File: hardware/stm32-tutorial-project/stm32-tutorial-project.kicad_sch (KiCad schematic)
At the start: 25 parts, among them J2 10pin IDC SWD, SW1 SW_Push, SW2 SW_Push_SPDT, U1 STM32G431CBTx

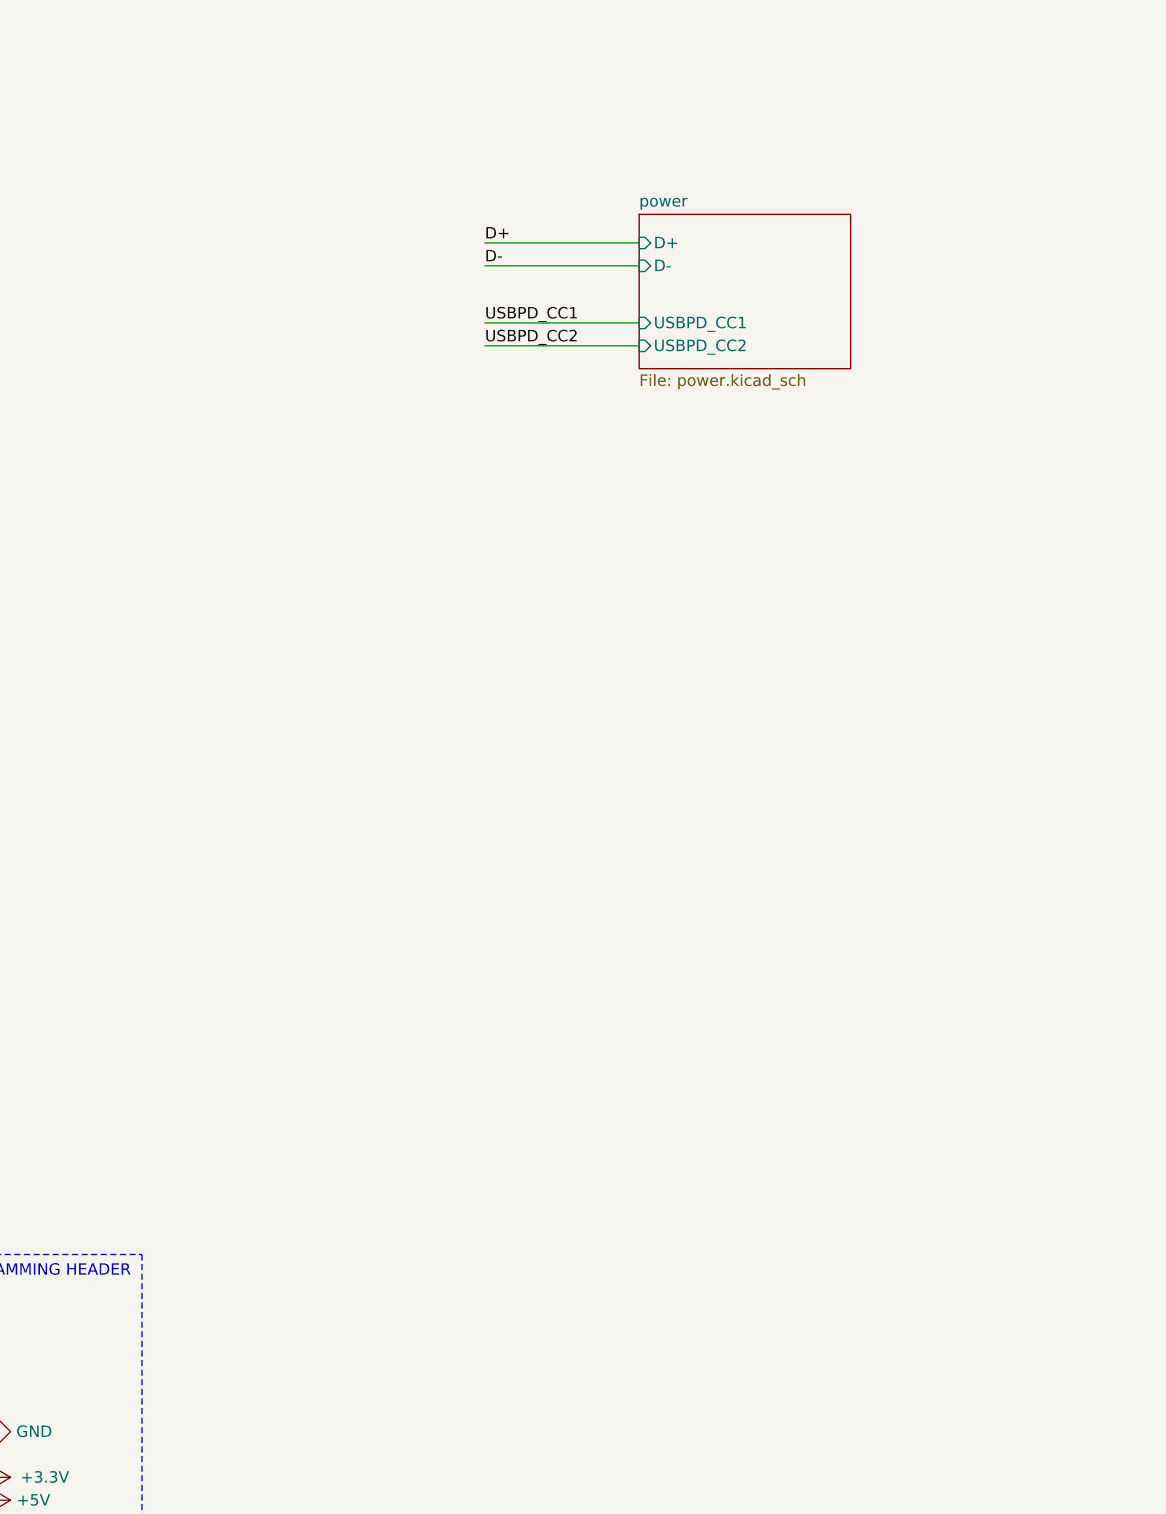
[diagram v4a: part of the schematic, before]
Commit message: added debug leds
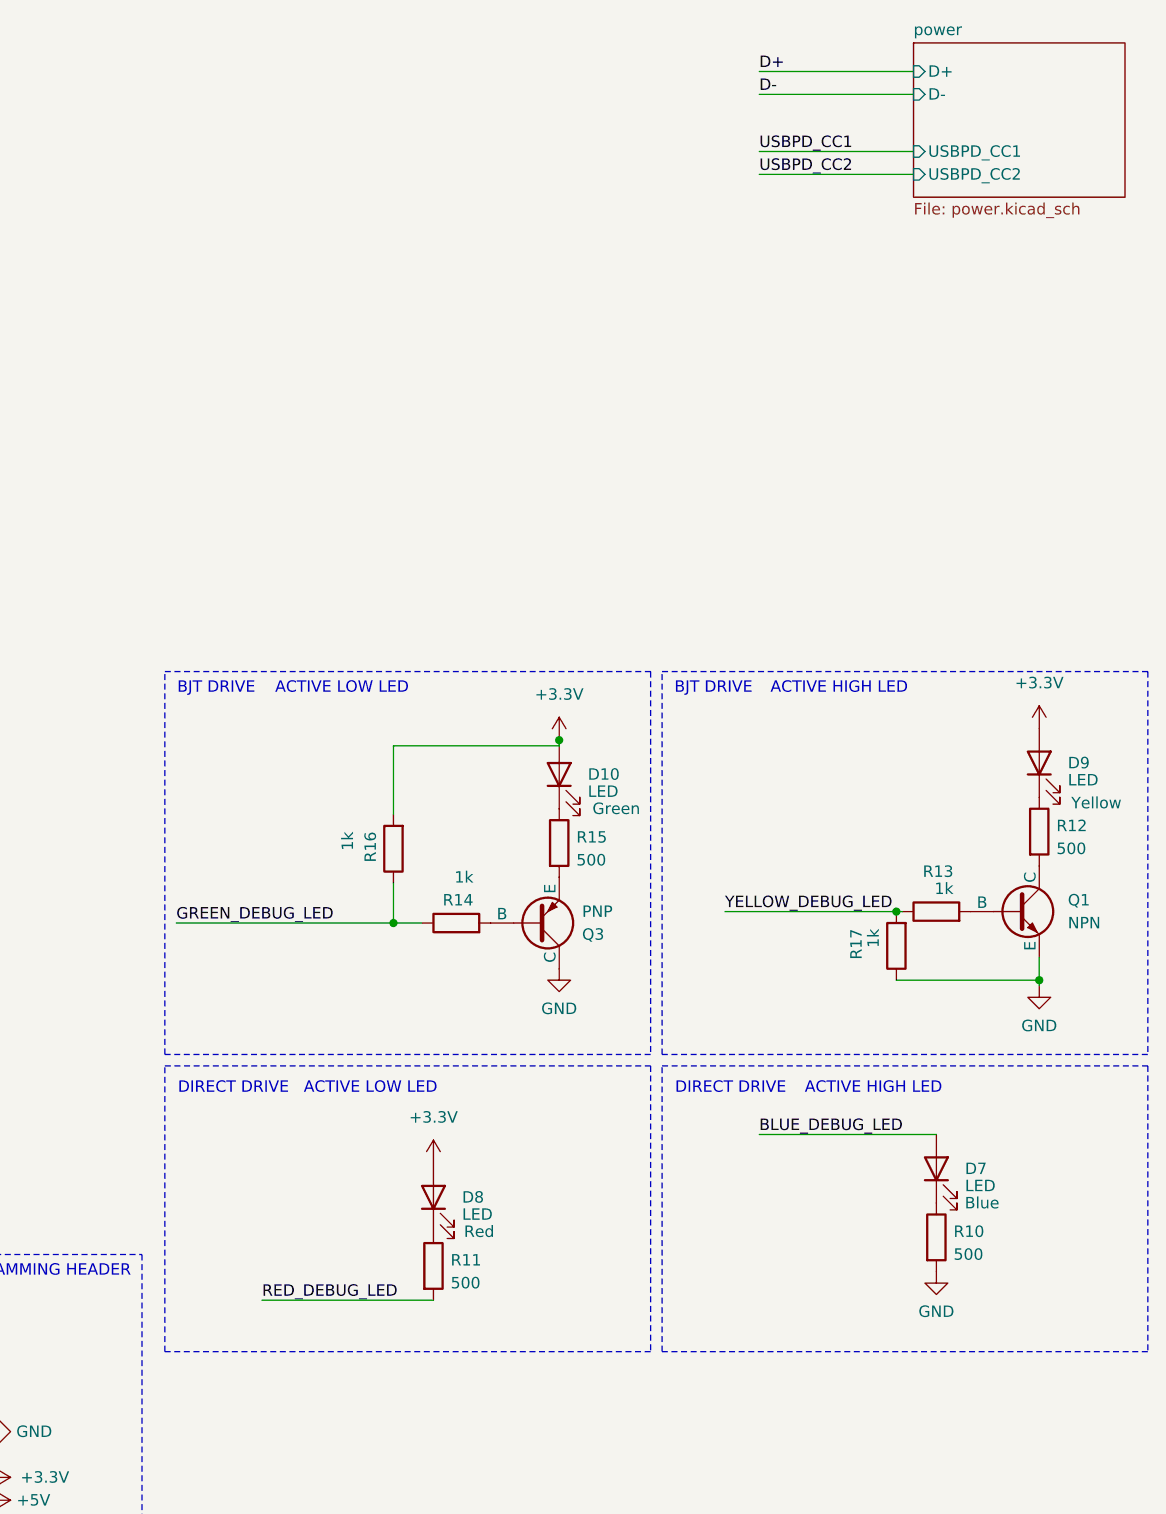
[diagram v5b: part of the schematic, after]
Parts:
- added D10, D7, D8, D9: LED, symbol Device:LED
- added Q1: NPN, symbol Simulation_SPICE:NPN
- added Q3: PNP, symbol Simulation_SPICE:PNP
- added R10, R11, R12, R15: 500, symbol Device:R
- added R13, R14, R16, R17: 1k, symbol Device:R
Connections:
- net +3.3V: now also D10.2 (A), D8.2 (A), D9.2 (A), R16.2
- net GND: now also Q1.3 (E), Q3.1 (C), R10.2, R17.1
- new net: D7.1 (K), R10.1
- new net: Q1.2 (B), R13.2
- new net: D8.1 (K), R11.1
- new net: D9.1 (K), R12.1
- new net: Q1.1 (C), R12.2
- new net: D10.1 (K), R15.1
- new net: Q3.3 (E), R15.2
- new net: Q3.2 (B), R14.2
- new net BLUE_DEBUG_LED: D7.2 (A)
- new net GREEN_DEBUG_LED: R14.1, R16.1
- new net RED_DEBUG_LED: R11.2
- new net YELLOW_DEBUG_LED: R13.1, R17.2
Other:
- note added: "ACTIVE HIGH LED"
- note added: "ACTIVE LOW LED"
- note added: "BJT DRIVE"
- note added: "DIRECT DRIVE"

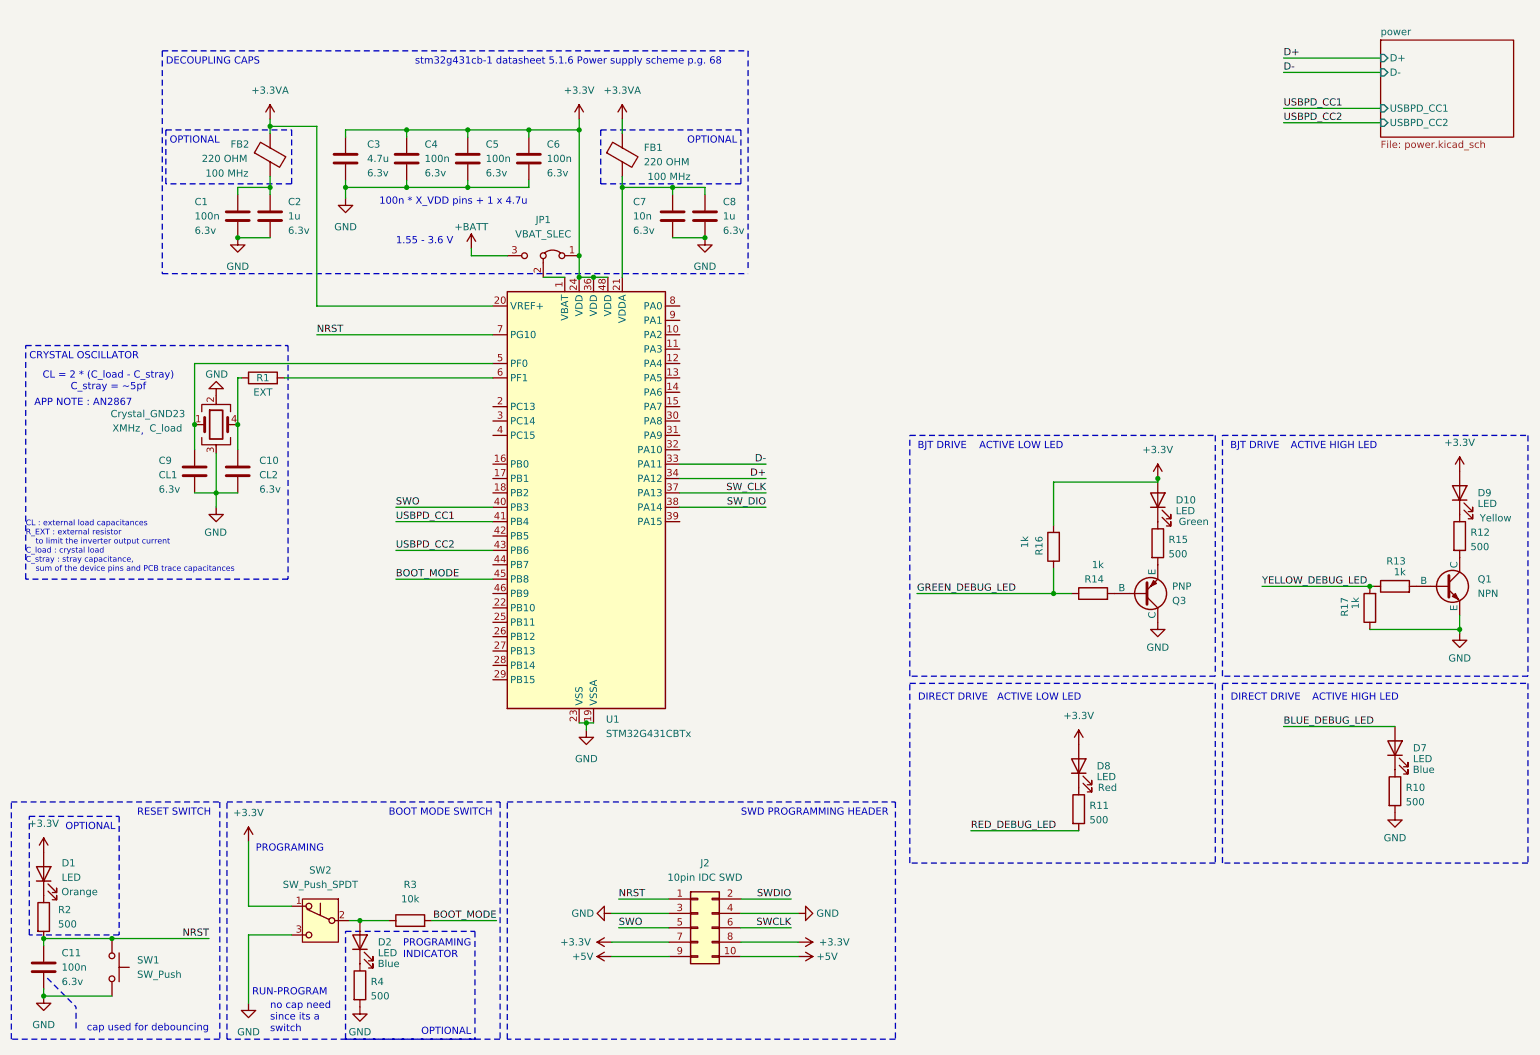
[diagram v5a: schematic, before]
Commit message: added connectors for distance sensors
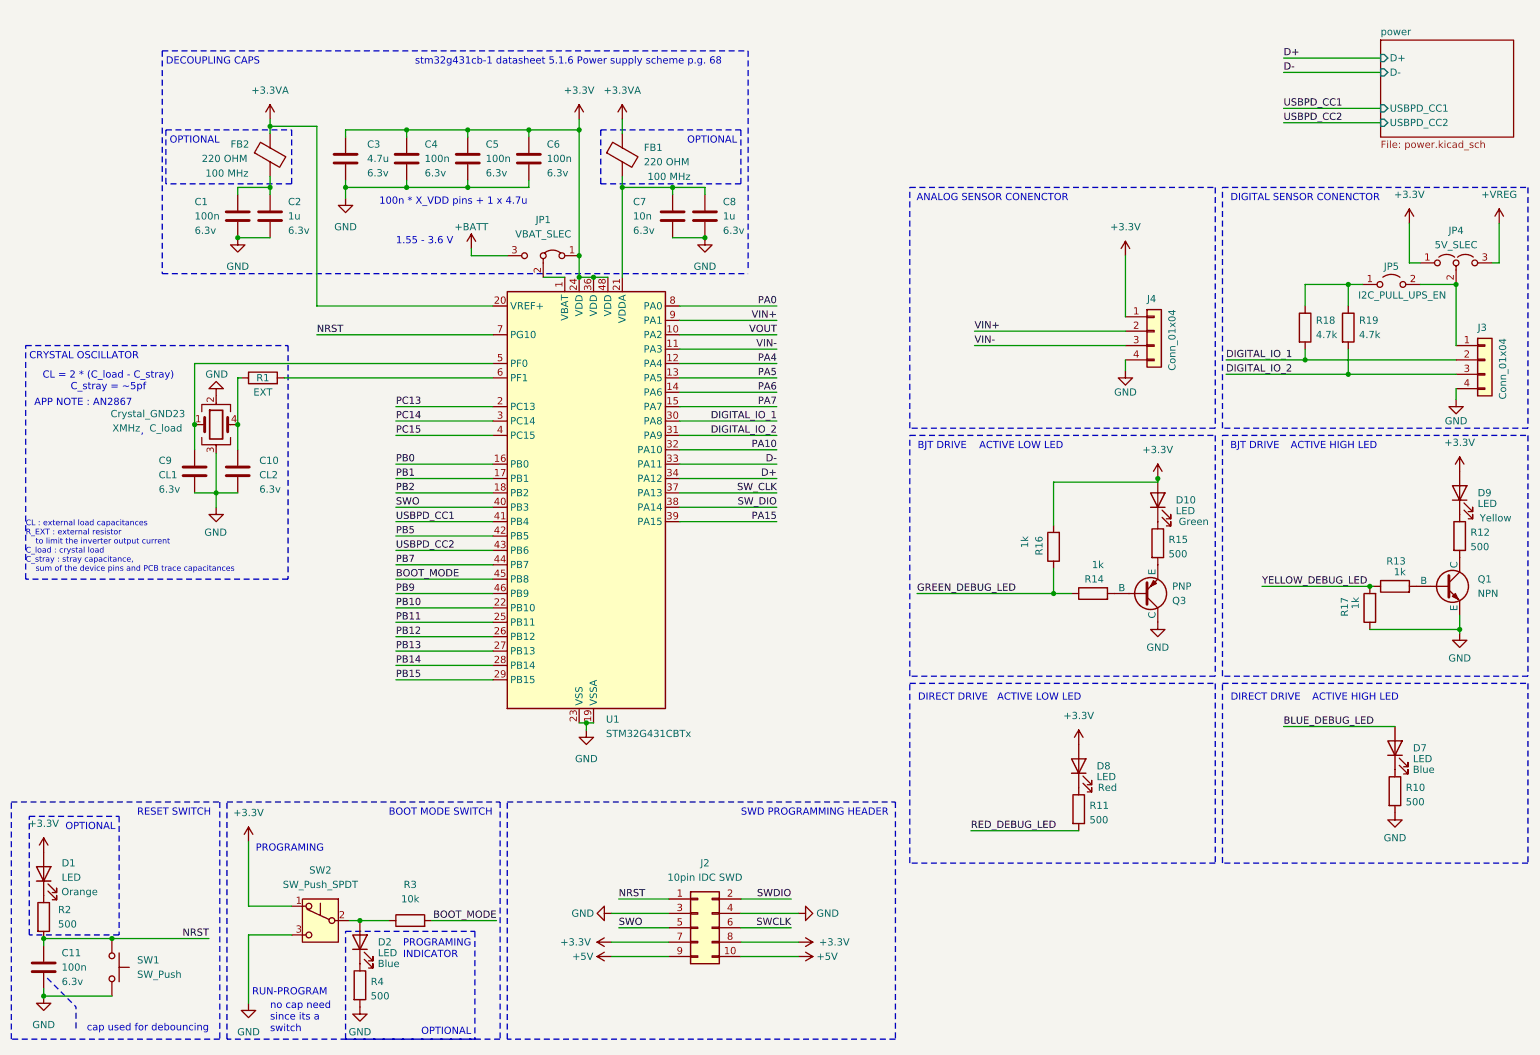
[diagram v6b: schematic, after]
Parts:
- added J3, J4: Conn_01x04, 4ms_Connector:Pins_1x04_2.54mm_TH_SWD, symbol PCM_4ms_Connector:Conn_01x04
- added JP4: 5V_SLEC, symbol Jumper:Jumper_3_Open
- added JP5: I2C_PULL_UPS_EN, symbol Jumper:Jumper_2_Open
- added R18, R19: 4.7k, symbol Device:R
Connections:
- net +3.3V: now also J4.1 (Pin_1), JP4.1 (A)
- net GND: now also J3.4 (Pin_4), J4.4 (Pin_4)
- net VOUT: now reaches U1.10 (PA2)
- net VIN-: now reaches U1.11 (PA3)
- net VIN-: now also J4.3 (Pin_3)
- net PA4: now reaches U1.12 (PA4)
- net PA5: now reaches U1.13 (PA5)
- net PA6: now reaches U1.14 (PA6)
- net PA7: now reaches U1.15 (PA7)
- net PB0: now reaches U1.16 (PB0)
- net PB1: now reaches U1.17 (PB1)
- net PB2: now reaches U1.18 (PB2)
- net PC13: now reaches U1.2 (PC13)
- net PB10: now reaches U1.22 (PB10)
- net PB11: now reaches U1.25 (PB11)
- net PB12: now reaches U1.26 (PB12)
- net PB13: now reaches U1.27 (PB13)
- net PB14: now reaches U1.28 (PB14)
- net PB15: now reaches U1.29 (PB15)
- net PC14: now reaches U1.3 (PC14)
- net DIGITAL_IO_1: now reaches U1.30 (PA8)
- net DIGITAL_IO_1: now also J3.2 (Pin_2), R18.2
- net DIGITAL_IO_2: now reaches U1.31 (PA9)
- net DIGITAL_IO_2: now also J3.3 (Pin_3), R19.2
- net PA10: now reaches U1.32 (PA10)
- net PA15: now reaches U1.39 (PA15)
- net PC15: now reaches U1.4 (PC15)
- net PB5: now reaches U1.42 (PB5)
- net PB7: now reaches U1.44 (PB7)
- net PB9: now reaches U1.46 (PB9)
- net PA0: now reaches U1.8 (PA0)
- net VIN+: now reaches U1.9 (PA1)
- net VIN+: now also J4.2 (Pin_2)
- new net: J3.1 (Pin_1), JP4.2 (C), JP5.2 (B)
- new net: JP5.1 (A), R18.1, R19.1
- new net +VREG: JP4.3 (B)
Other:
- note added: "ANALOG SENSOR CONENCTOR"
- note added: "DIGITAL SENSOR CONENCTOR"

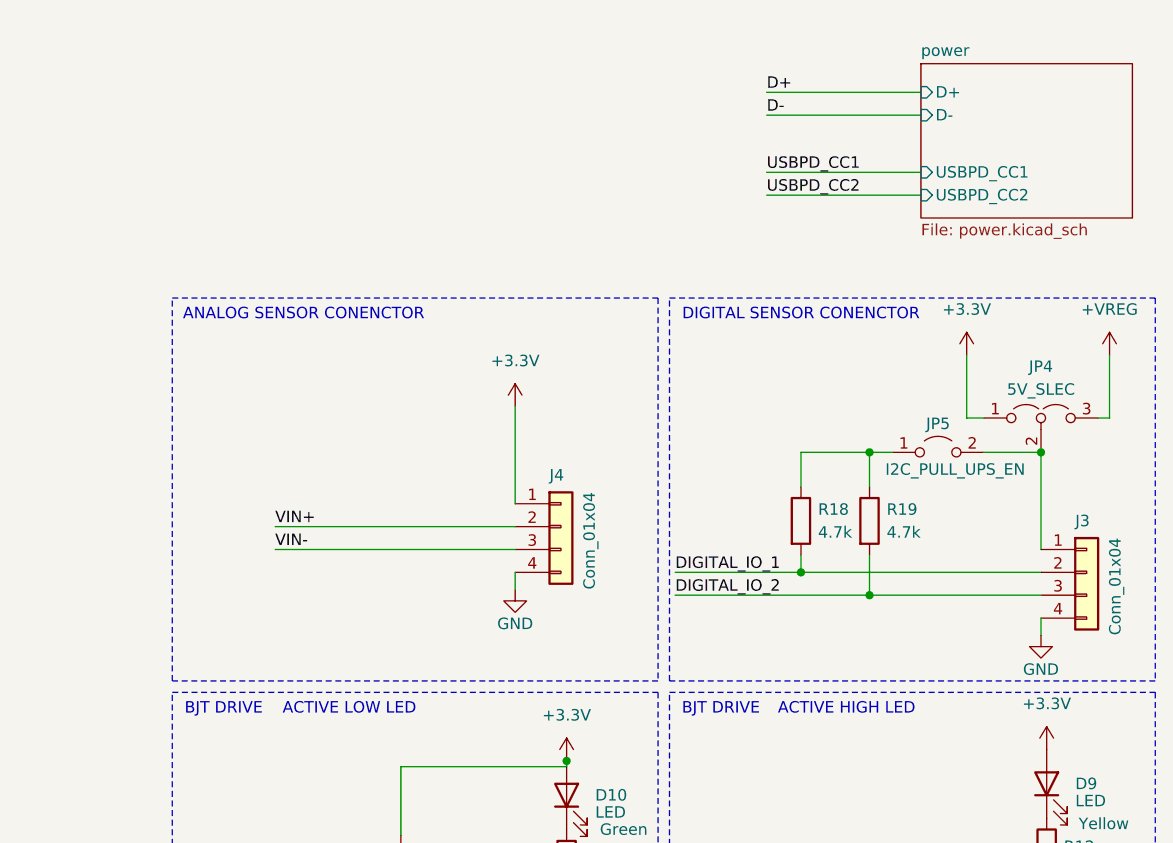
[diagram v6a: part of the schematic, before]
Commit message: added connectors for extra pins
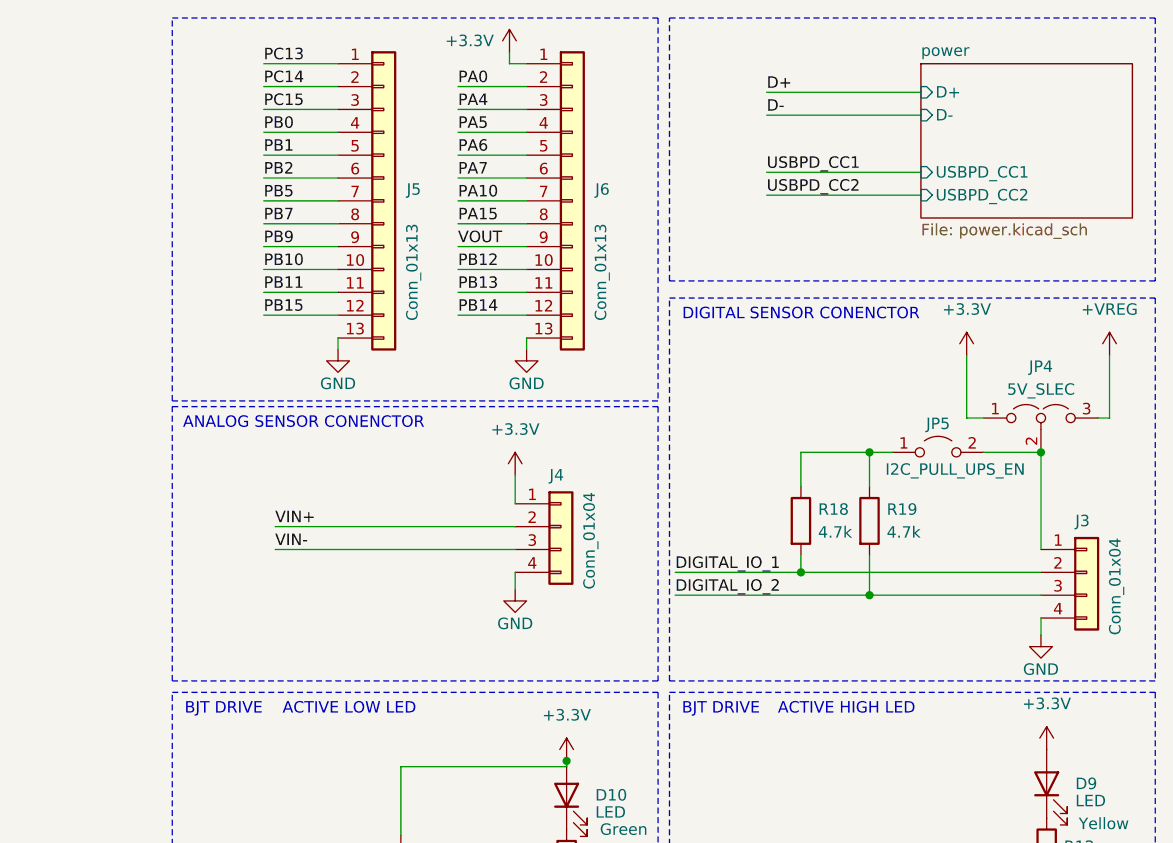
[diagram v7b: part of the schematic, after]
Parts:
- added J5, J6: Conn_01x13, symbol Connector_Generic:Conn_01x13
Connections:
- net +3.3V: now also J6.1 (Pin_1)
- net GND: now also J5.13 (Pin_13), J6.13 (Pin_13)
- net PA0: now also J6.2 (Pin_2)
- net PA10: now also J6.7 (Pin_7)
- net PA15: now also J6.8 (Pin_8)
- net PA4: now also J6.3 (Pin_3)
- net PA5: now also J6.4 (Pin_4)
- net PA6: now also J6.5 (Pin_5)
- net PA7: now also J6.6 (Pin_6)
- net PB0: now also J5.4 (Pin_4)
- net PB1: now also J5.5 (Pin_5)
- net PB10: now also J5.10 (Pin_10)
- net PB11: now also J5.11 (Pin_11)
- net PB12: now also J6.10 (Pin_10)
- net PB13: now also J6.11 (Pin_11)
- net PB14: now also J6.12 (Pin_12)
- net PB15: now also J5.12 (Pin_12)
- net PB2: now also J5.6 (Pin_6)
- net PB5: now also J5.7 (Pin_7)
- net PB7: now also J5.8 (Pin_8)
- net PB9: now also J5.9 (Pin_9)
- net PC13: now also J5.1 (Pin_1)
- net PC14: now also J5.2 (Pin_2)
- net PC15: now also J5.3 (Pin_3)
- net VOUT: now also J6.9 (Pin_9)
